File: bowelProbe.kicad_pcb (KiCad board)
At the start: 2 copper layers, 119.8 x 64.8 mm, 53 parts, among them J10 Conn_01x01, J11 Conn_01x01, J12 Conn_01x01, J13 Conn_01x01, J2 Conn_01x01, J3 Conn_01x01, J4 Conn_01x01, J5 Conn_01x01, J6 Conn_01x01, J7 Conn_01x01, J8 Conn_01x01, J9 Conn_01x01, U1 MAX038CPP, U2 OPA2134PA, U3 MCP6002-E/P, U4 TL072ACP

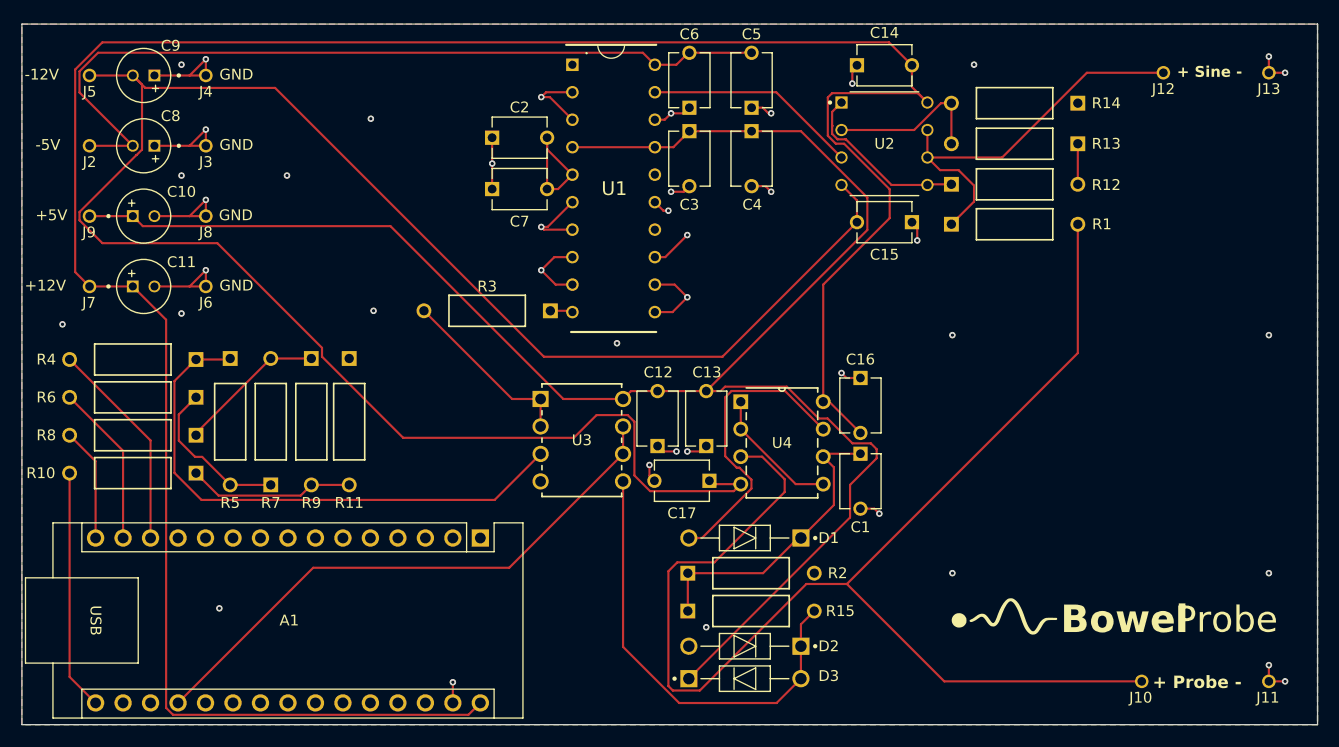
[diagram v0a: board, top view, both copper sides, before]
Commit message: PCB Passed Final Check
Updated PCB reference designators (both in schematic and layout). Gave final check to ensure proper PCB layout and routing.
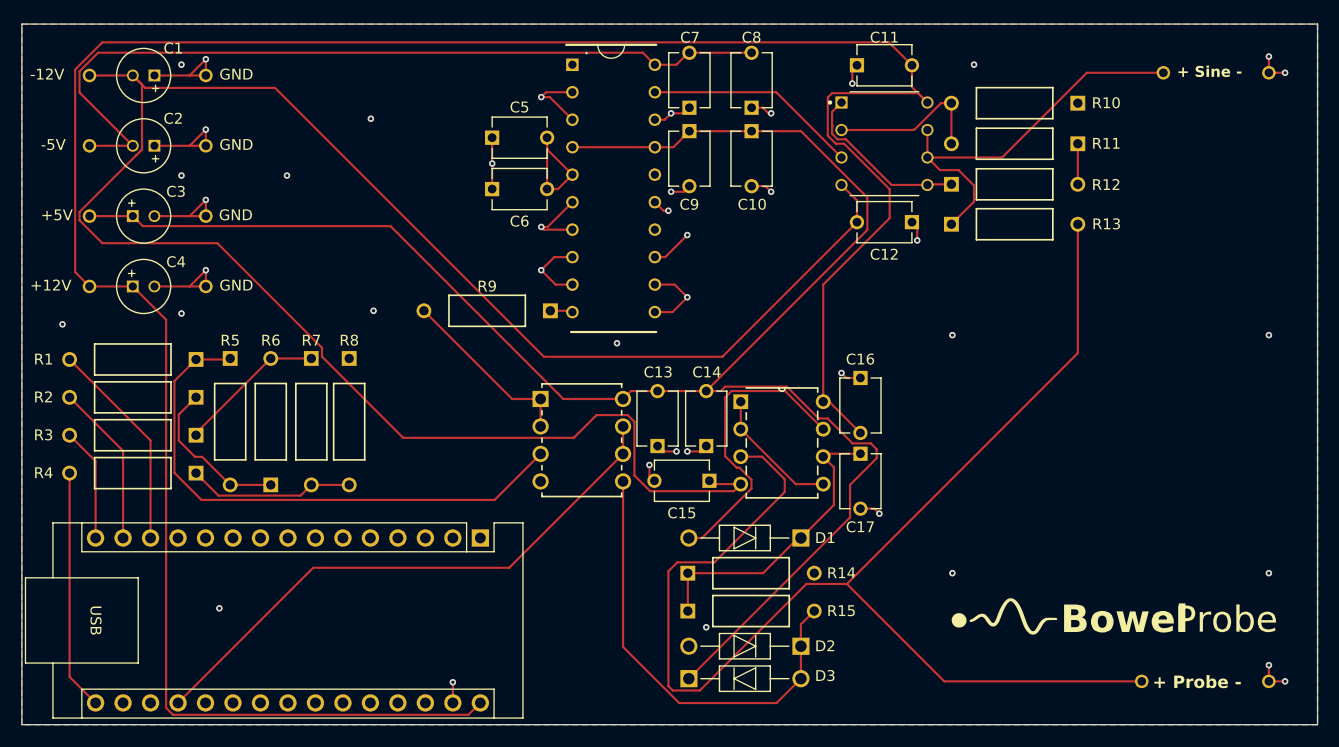
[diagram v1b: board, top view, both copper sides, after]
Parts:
- D1, D2, D3: value 1N5817 -> DIOAD1036W78L470D235
- renumbered C9 to C1, C4 to C10, C14 to C11, C15 to C12, C12 to C13, C13 to C14, C17 to C15, C1 to C17, C8 to C2, C10 to C3, C11 to C4, C2 to C5, C7 to C6, C6 to C7, C5 to C8, C3 to C9, R4 to R1, R14 to R10, R13 to R11, R1 to R13, R2 to R14, R6 to R2, R8 to R3, R10 to R4, R7 to R6, R9 to R7, R11 to R8, R3 to R9
